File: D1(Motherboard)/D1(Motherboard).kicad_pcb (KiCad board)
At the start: 4 copper layers, 38 x 35 mm, 71 parts, among them J1 WR-FPC_0.5mm_ZIF_V, J2 USB_C_Receptacle_USB2.0, J3 B2B-PH-K-S, Q1 NX2301P.215, SW1 CHS-02A, U1 ESP32-S2, U2 ICM-20602, U3 WR-FPC_0.5mm_ZIF_H, U4 MIC5353-3.3YMT, U5 FAN5331SX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

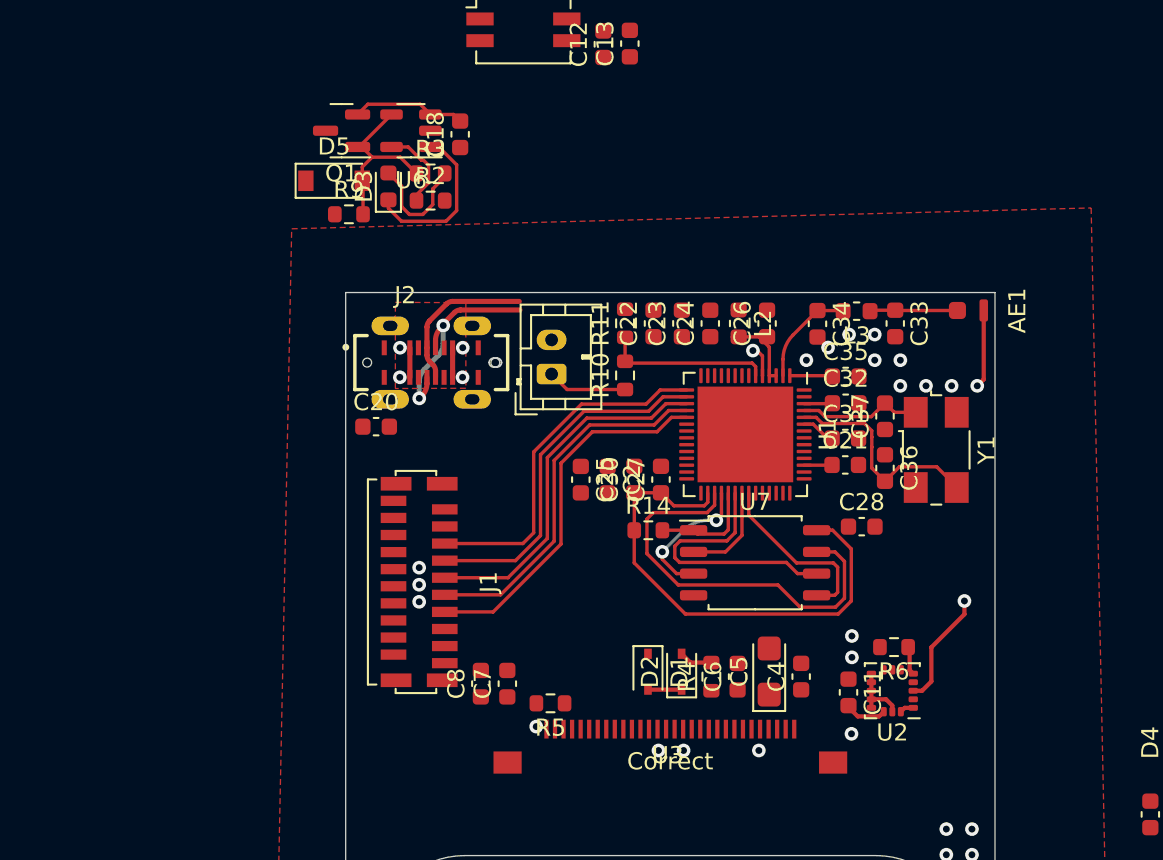
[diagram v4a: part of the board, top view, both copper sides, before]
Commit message: Changed antenna symbol and removed ground from pin + more layout
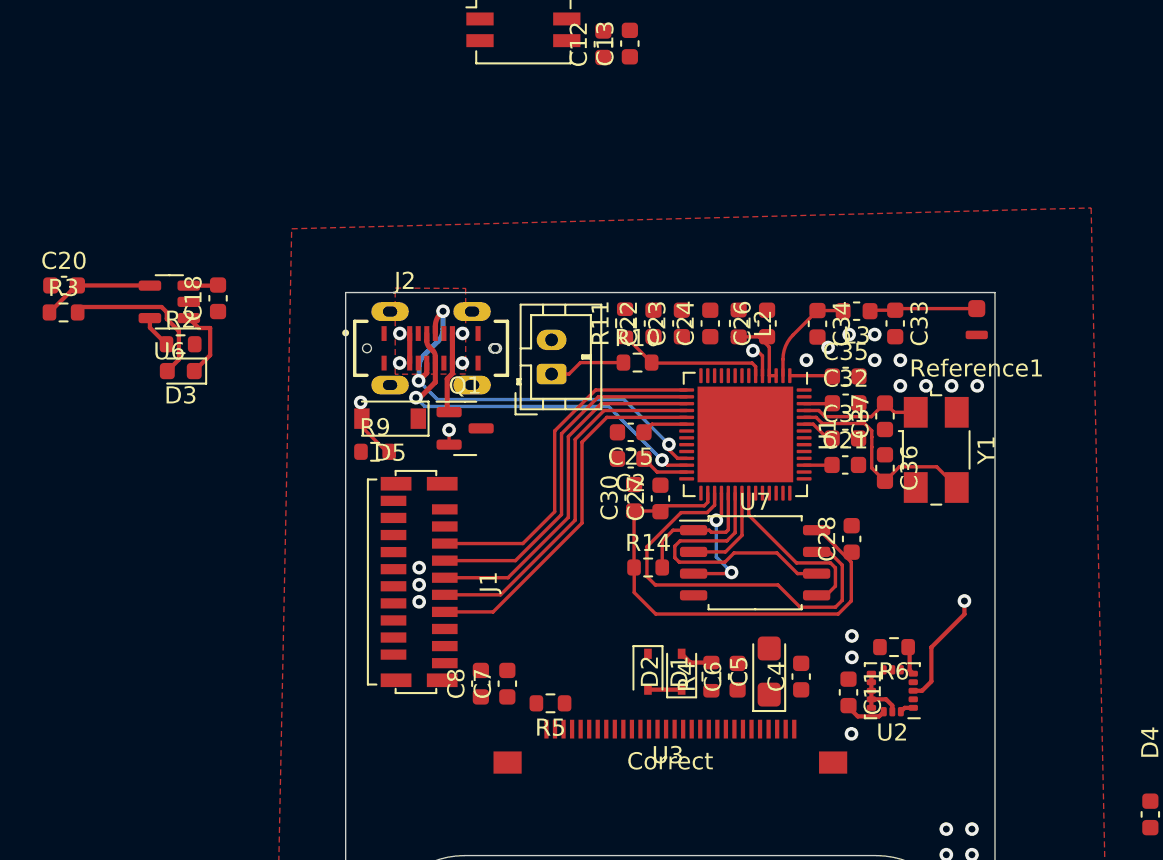
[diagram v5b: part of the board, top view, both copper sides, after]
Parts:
- removed AE1: Antenna_Chip, Ignion_Antenna:NN02-101
- added Reference1: Ignion-NN02-101, Ignion_Antenna:NN02-101, F.Cu at (70.6, 33.6)
- moved R3 23.0 mm to (17.1, 33.0)
- moved C20 20.0 mm to (17.1, 31.4)
- moved Q1 18.9 mm to (40.6, 39.8), turned to 0 degrees
- moved U6 17.3 mm to (23.3, 32.4)
- moved C18 17.1 mm to (26.2, 32.2)
- moved R2 16.9 mm to (24.0, 34.9)
- moved D3 16.3 mm to (24.0, 36.4), turned to 180 degrees
- moved D5 14.3 mm to (36.2, 39.2), turned to 180 degrees
- moved R9 14.0 mm to (35.3, 41.2)
- moved C25 4.02 mm to (50.3, 40.0), turned to 180 degrees
- moved R14 2.18 mm to (51.3, 47.9)
- moved C2 1.82 mm to (50.3, 41.6), turned to 180 degrees
- moved C27 1.11 mm to (52.0, 43.9)
- moved C30 1.07 mm to (50.5, 43.8)
- moved R10 1.05 mm to (50.7, 35.9), turned to 0 degrees
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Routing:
- net D-: track 12.5 -> 25.3 mm, vias 2 -> 3
- net D+: track 9.20 -> 22.0 mm, vias 0 -> 2
- net +3V3: track 13.5 -> 19.0 mm
- net Net-(D3-Pad1): track 9.70 -> 4.40 mm
- net GND: track 13.7 -> 8.93 mm, vias 21 -> 17
- net +BATT: track 11.3 -> 7.07 mm, vias 0 -> 1
- net Net-(R2-Pad1): track 4.97 -> 1.93 mm
- net Net-(D3-Pad2): track 6.65 -> 9.49 mm
- net VBUS: track 14.1 -> 16.9 mm, vias 4 -> 5
- net SPICS0: track 6.20 -> 7.93 mm
- net VDD_SPI: track 29.9 -> 28.5 mm
- net Net-(C33-Pad1): track 5.14 -> 6.33 mm
- net Net-(R10-Pad2): track 9.70 -> 8.88 mm
- net SPIWP: track 8.16 -> 7.38 mm
- added copper zone on In1.Cu, net +BATT

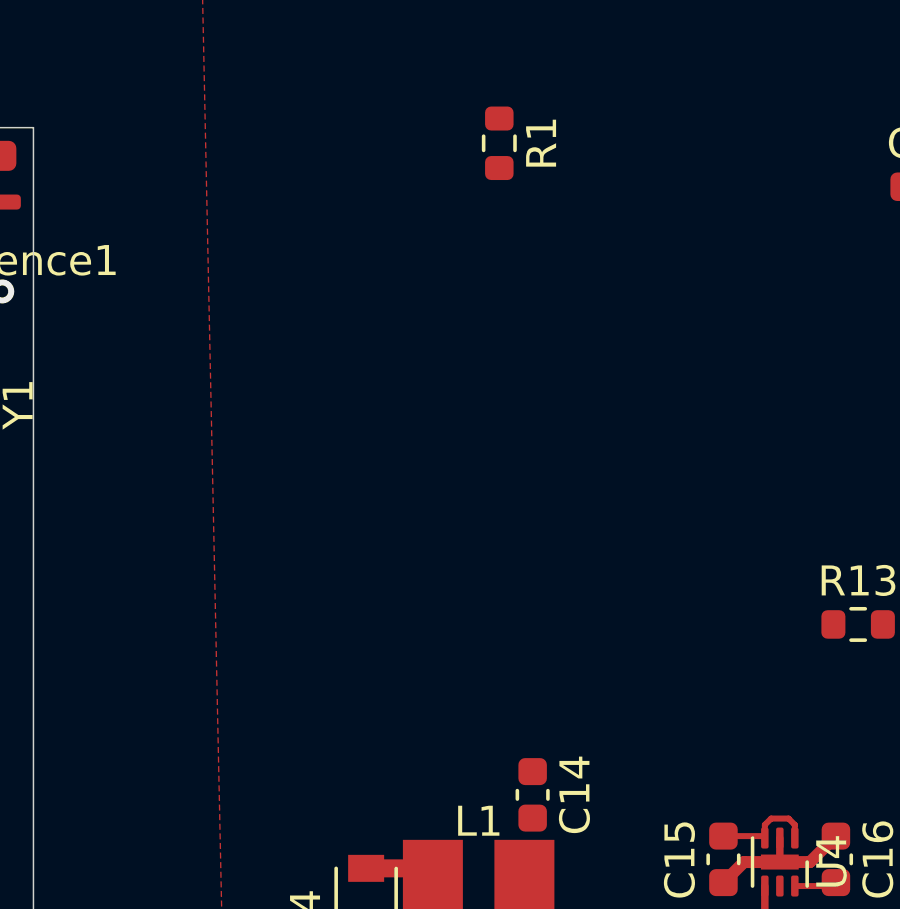
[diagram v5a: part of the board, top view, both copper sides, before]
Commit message: Potentially move over to ESP32-S2-MINI-1U
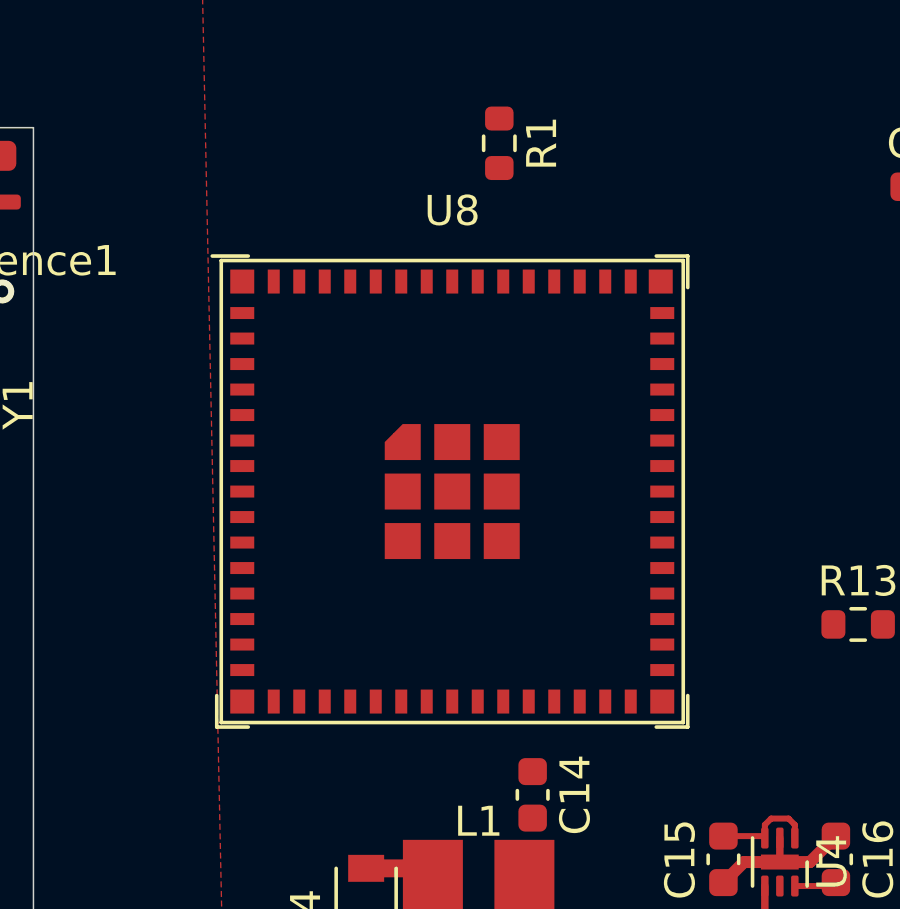
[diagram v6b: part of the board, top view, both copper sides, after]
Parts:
- added U8: ESP32-S2-MINI-1, Espressif:ESP32-S2-MINI-1U, F.Cu at (85.6, 44.0)

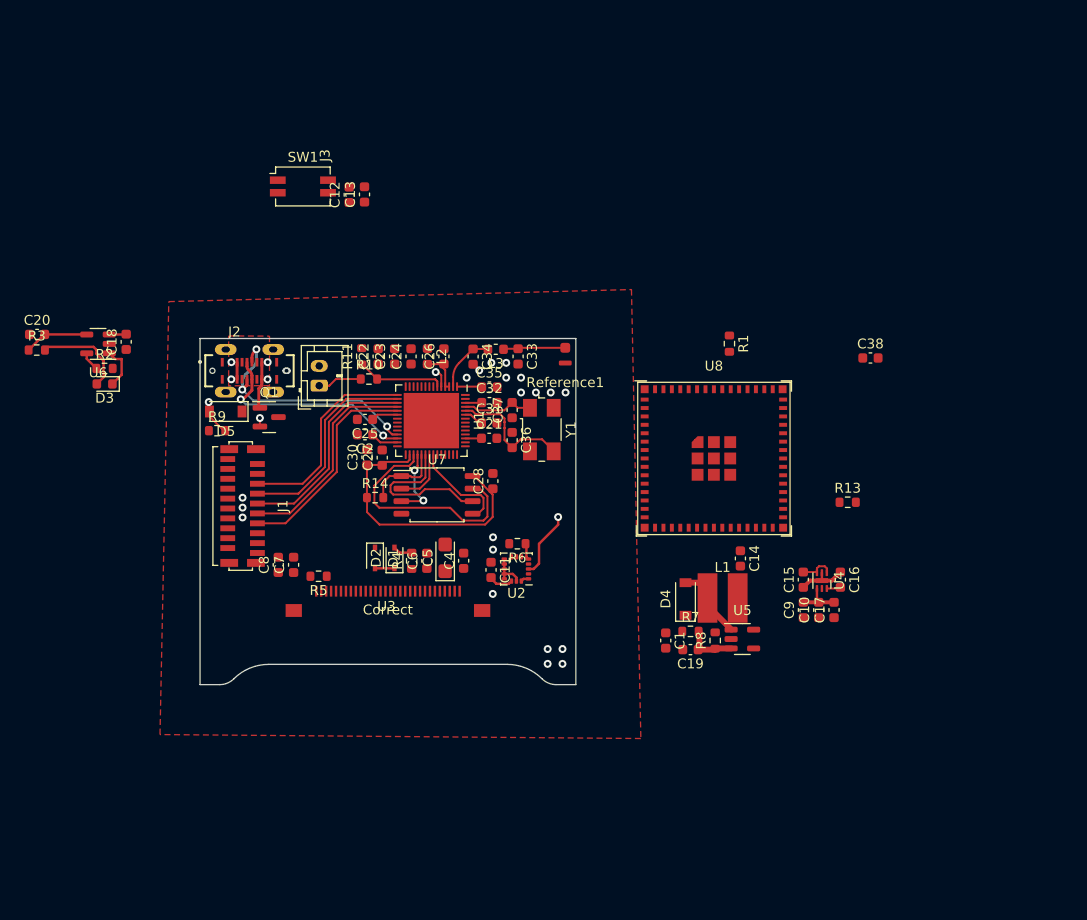
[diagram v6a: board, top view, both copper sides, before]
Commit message: Made changed to layout to match available space with S2 Mini 1U
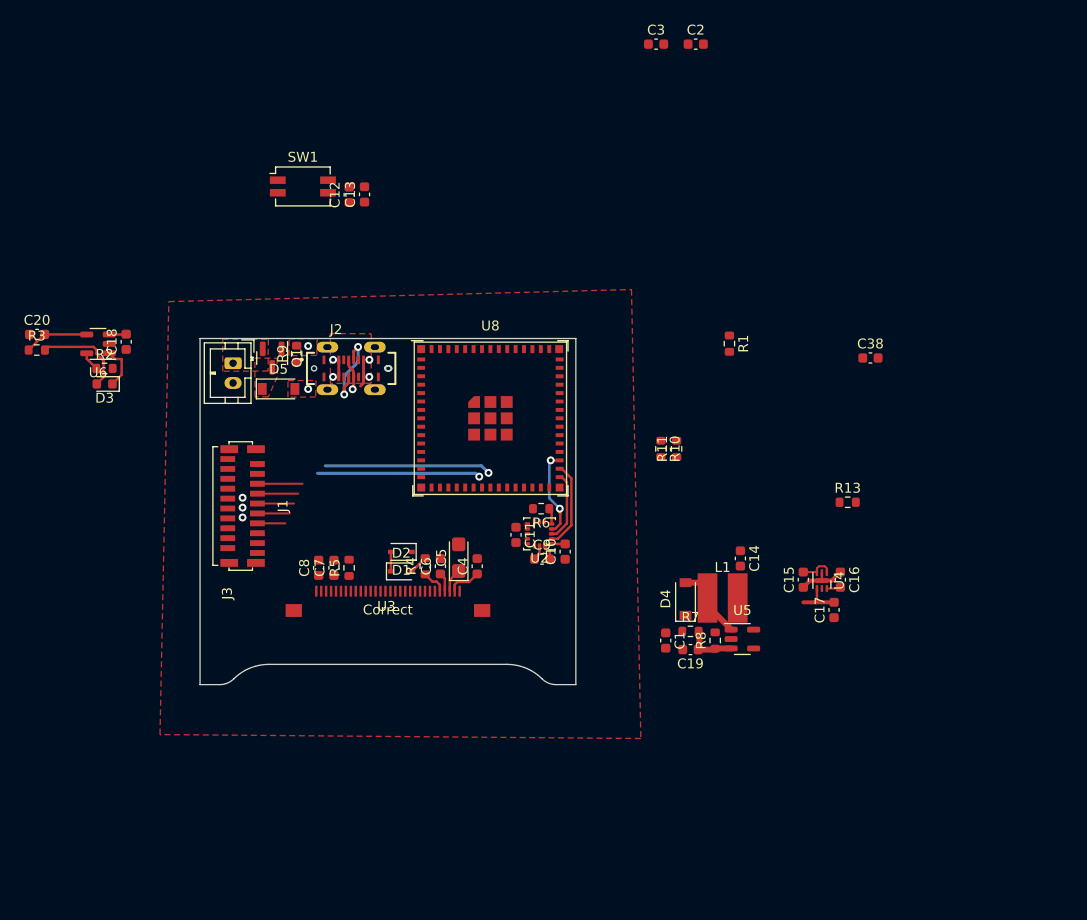
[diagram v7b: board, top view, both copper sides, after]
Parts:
- removed C21, C24, C25, C27, C28, C35: 0.1u, Capacitor_SMD:C_0603_1608Metric
- removed C22: 10u, Capacitor_SMD:C_0603_1608Metric
- removed C23: 1u, Capacitor_SMD:C_0603_1608Metric
- removed C26, C33, C34, C36, C37: TBD, Capacitor_SMD:C_0603_1608Metric
- removed C30, C32: 1uF, Capacitor_SMD:C_0603_1608Metric
- removed C31: 100pF, Capacitor_SMD:C_0603_1608Metric
- removed L2: 2n, Inductor_SMD:L_0603_1608Metric
- removed L3: TBD, Inductor_SMD:L_0603_1608Metric
- removed R14: 10k(NC), Resistor_SMD:R_0603_1608Metric
- removed Reference1: Ignion-NN02-101, Ignion_Antenna:NN02-101
- removed U1: ESP32-S2, Package_DFN_QFN:QFN-56-1EP_7x7mm_P0.4mm_EP5.6x5.6mm
- removed U7: W25Q128JVS, Package_SO:SOIC-8_5.23x5.23mm_P1.27mm
- removed Y1: Crystal_GND24, Crystal:Crystal_SMD_0603-4Pin_6.0x3.5mm
- added C3: 0.1u, Capacitor_SMD:C_0603_1608Metric, F.Cu at (79.7, 2.07)
- U3: value WR-FPC_0.5mm_ZIF_H -> 687130183622
- moved C2 51.8 mm to (83.8, 2.07), turned to 0 degrees
- moved R11 33.2 mm to (81.8, 43.0)
- moved R10 30.4 mm to (80.2, 43.0), turned to -90 degrees
- moved C9 26.9 mm to (68.2, 54.1), turned to 0 degrees
- moved C10 26.3 mm to (70.5, 53.4)
- moved U8 23.0 mm to (63.0, 39.9)
- moved R9 11.2 mm to (43.4, 33.4), turned to 90 degrees
- moved J2 10.3 mm to (48.9, 34.9)
- moved J3 9.00 mm to (37.0, 34.3), turned to -90 degrees
- moved Q1 5.98 mm to (40.9, 33.8), turned to -90 degrees
- moved D5 5.81 mm to (41.6, 36.9), turned to 0 degrees
- moved C11 4.35 mm to (65.6, 51.7)
- moved R6 4.28 mm to (68.1, 49.0)
- moved U2 4.25 mm to (68.0, 51.6)
- moved C8 4.09 mm to (45.6, 55.0)
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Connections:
- U8 pad 1: unconnected-(U8-Pad1) -> GND
- U8 pad 10: unconnected-(U8-Pad10) -> INT
- U8 pad 11: unconnected-(U8-Pad11) -> RST
- U8 pad 12: unconnected-(U8-Pad12) -> DC
- U8 pad 13: unconnected-(U8-Pad13) -> Display1_CS
- U8 pad 14: unconnected-(U8-Pad14) -> Display2_CS
- U8 pad 15: unconnected-(U8-Pad15) -> Display3_CS
- U8 pad 16: unconnected-(U8-Pad16) -> Display4_CS
- U8 pad 17: unconnected-(U8-Pad17) -> Display5_CS
- U8 pad 18: unconnected-(U8-Pad18) -> Display6_CS
- U8 pad 2: unconnected-(U8-Pad2) -> GND
- U8 pad 23: unconnected-(U8-Pad23) -> D-
- U8 pad 24: unconnected-(U8-Pad24) -> D+
- U8 pad 3: unconnected-(U8-Pad3) -> +3V3
- U8 pad 30: unconnected-(U8-Pad30) -> GND
- U8 pad 31: unconnected-(U8-Pad31) -> MOSI
- U8 pad 32: unconnected-(U8-Pad32) -> CLK
- U8 pad 33: unconnected-(U8-Pad33) -> MISO
- U8 pad 39: unconnected-(U8-Pad39) -> Net-(R13-Pad1)
- U8 pad 4: unconnected-(U8-Pad4) -> Boot
- U8 pad 40: unconnected-(U8-Pad40) -> U0RXD
- U8 pad 42: unconnected-(U8-Pad42) -> GND
- U8 pad 43: unconnected-(U8-Pad43) -> GND
- U8 pad 45: unconnected-(U8-Pad45) -> Reset
- U8 pad 46: unconnected-(U8-Pad46) -> GND
- U8 pad 5: unconnected-(U8-Pad5) -> Net-(R10-Pad2)
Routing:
- net VDD_SPI: track 28.5 -> 0.00 mm
- net SPIHD: track 23.6 -> 0.00 mm
- net Display6_CS: track 21.6 -> 2.83 mm
- net Display5_CS: track 21.4 -> 3.26 mm
- net Display4_CS: track 21.1 -> 3.70 mm
- net Display3_CS: track 20.9 -> 4.13 mm
- net D-: track 25.3 -> 8.84 mm, vias 3 -> 2
- net Display2_CS: track 20.6 -> 4.57 mm
- net SPICLK: track 16.0 -> 0.00 mm
- net GND: track 8.93 -> 23.4 mm, vias 17 -> 1
- net XTAL_N: track 12.6 -> 0.00 mm
- net SPID: track 10.0 -> 0.00 mm
- net MISO: track 0.00 -> 8.94 mm, vias 0 -> 2
- net CLK: track 0.00 -> 8.91 mm
- net Net-(R10-Pad2): track 8.88 -> 0.00 mm
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- added copper zone on F.Cu, net +5V
- added copper zone on F.Cu, net +BATT
- removed copper zone on In1.Cu, net +BATT

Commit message: More layout work
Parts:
- removed R13: 499R, Resistor_SMD:R_0603_1608Metric
- added D6: GREEN, LED_SMD:LED_0603_1608Metric, F.Cu at (57.8, 49.5)
- added R12: 1k, Resistor_SMD:R_0603_1608Metric, F.Cu at (56.2, 49.5)
- U3: value 687130183622 -> SSD1351
- moved C2 48.4 mm to (52.8, 39.3), turned to -90 degrees
- moved C3 46.9 mm to (51.3, 39.3), turned to -90 degrees
- moved C21 31.1 mm to (70.5, 36.9), turned to -90 degrees
- moved R3 30.1 mm to (46.3, 40.4)
- moved C20 30.1 mm to (46.3, 38.9), turned to 180 degrees
- moved R11 23.4 mm to (59.3, 49.5), turned to -90 degrees
- moved R2 20.7 mm to (44.1, 39.6), turned to -90 degrees
- moved R10 20.4 mm to (60.9, 49.5), turned to 90 degrees
- moved U6 19.4 mm to (41.2, 39.9), turned to 0 degrees
- moved D3 19.3 mm to (42.3, 42.4), turned to 0 degrees
- moved R1 16.7 mm to (70.5, 33.9)
- moved C18 13.6 mm to (37.6, 39.6), turned to 180 degrees
- moved C13 4.70 mm to (46.1, 19.6), turned to 180 degrees
- moved C12 4.68 mm to (46.1, 13.4), turned to 180 degrees
- moved U1 1.30 mm to (61.7, 39.9)
- renumbered C38 to C21, U8 to U1
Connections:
- U1 pad 10: INT -> DC
- U1 pad 11: RST -> Display1_CS
- U1 pad 12: DC -> Display2_CS
- U1 pad 13: Display1_CS -> Display3_CS
- U1 pad 14: Display2_CS -> Display4_CS
- U1 pad 15: Display3_CS -> Display5_CS
- U1 pad 16: Display4_CS -> Display6_CS
- U1 pad 17: Display5_CS -> Net-(U1-Pad17)
- U1 pad 18: Display6_CS -> Net-(R10-Pad2)
- U1 pad 39: Net-(R13-Pad1) -> unconnected-(U1-Pad39)
- U1 pad 40: U0RXD -> unconnected-(U1-Pad40)
- U1 pad 5: Net-(R10-Pad2) -> unconnected-(U1-Pad5)
- U1 pad 8: unconnected-(U8-Pad8) -> INT
- U1 pad 9: unconnected-(U8-Pad9) -> RST
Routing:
- net Display6_CS: track 2.83 -> 18.0 mm
- net Display3_CS: track 4.13 -> 18.1 mm
- net Display4_CS: track 3.70 -> 17.7 mm
- net Display5_CS: track 3.26 -> 17.3 mm
- net Display2_CS: track 4.57 -> 18.6 mm
- net Net-(D3-Pad2): track 9.49 -> 0.00 mm
- net +BATT: track 1.73 -> 9.96 mm
- net VBUS: track 11.2 -> 4.51 mm
- net Net-(R10-Pad2): track 0.00 -> 4.28 mm
- net Net-(D6-Pad2): track 0.00 -> 2.25 mm
- net Net-(U1-Pad17): track 0.00 -> 1.88 mm
- net GND: track 23.4 -> 25.3 mm
- net CLK: track 8.91 -> 10.2 mm
- net MOSI: track 7.10 -> 8.40 mm
